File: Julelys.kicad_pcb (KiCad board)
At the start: 4 copper layers, 65 x 56 mm, 118 parts, among them J1 Raspberry_Pi_40pin, J10 B3B-XH-A, J11 B3B-XH-A, J12 Conn_01x03_Pin, J13 FAN, J3 Conn_02x06_Odd_Even, J4 B3B-XH-A, J5 B3B-XH-A, J6 B3B-XH-A, J7 B3B-XH-A, J8 B3B-XH-A, J9 B3B-XH-A, P1 USB_C_Receptacle_USB2.0, Q1 AO3400A, SW1 SW_Push, SW2 SW_Push, U1 ESP32-C3-WROOM-02, U10 74LVC1G08, U2 74HC4051, U3 AMS1117-3.3, U4 BC847BDW1T1G, U5 CP2102N-A02-GQFN28, U6 74AHCT1G125, U7 74AHCT1G125, U8 74AHCT1G125, U9 74AHCT1G125

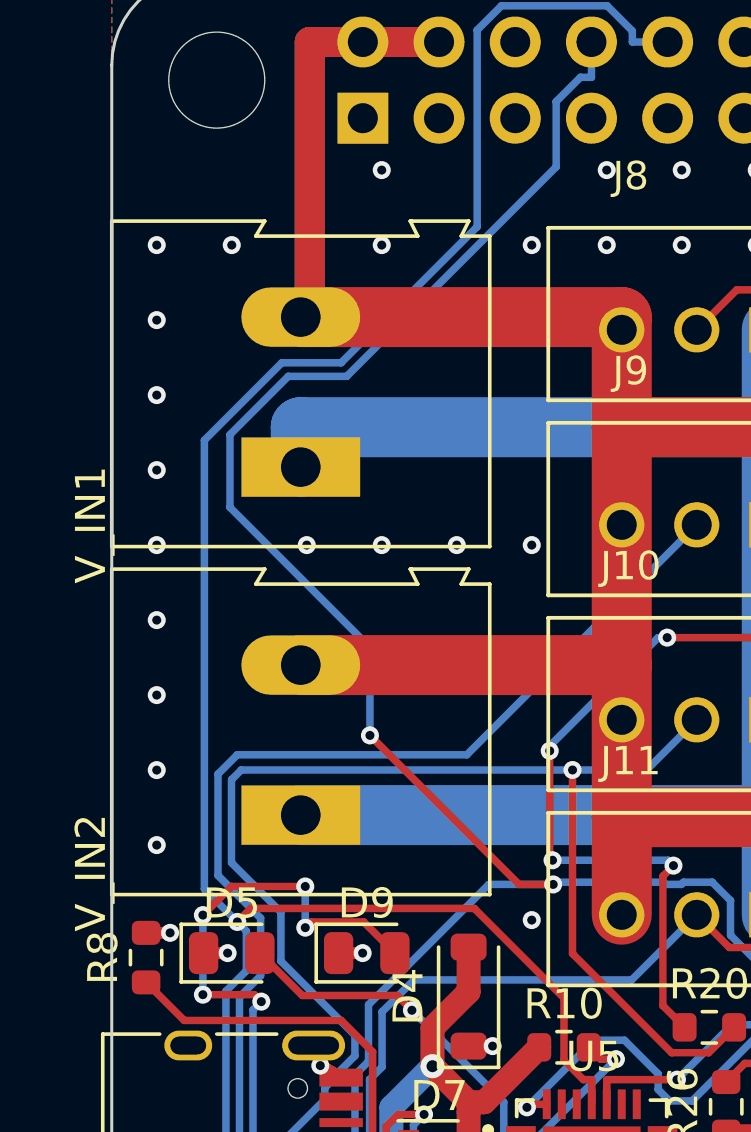
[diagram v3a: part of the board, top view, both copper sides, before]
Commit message: Add 3D models for all parts, turn screw terminals to face the board edge
- Point library parts at KiCad 10 STEP models; copy the HRO USB-C and
  ESP32-C3 models into 3D/ so the project is self-contained
- Add models for U2 (SOIC-16) and U5 (CP2102N); use the KiCad TL3305A
  model instead of a file in Downloads
- Rotate V_IN1/V_IN2 so the 45-degree wire entry faces the left edge;
  mirror the symbols (pin 1 = +5V, pin 2 = GND) so the power tracks stay
- Reroute TXD and PI_TX segments that came too close to the new pads
- Document Pi 5 Active Cooler mounting (GPIO extension, taller standoffs)

Co-Authored-By: Claude Opus 5.5 <noreply@anthropic.com>
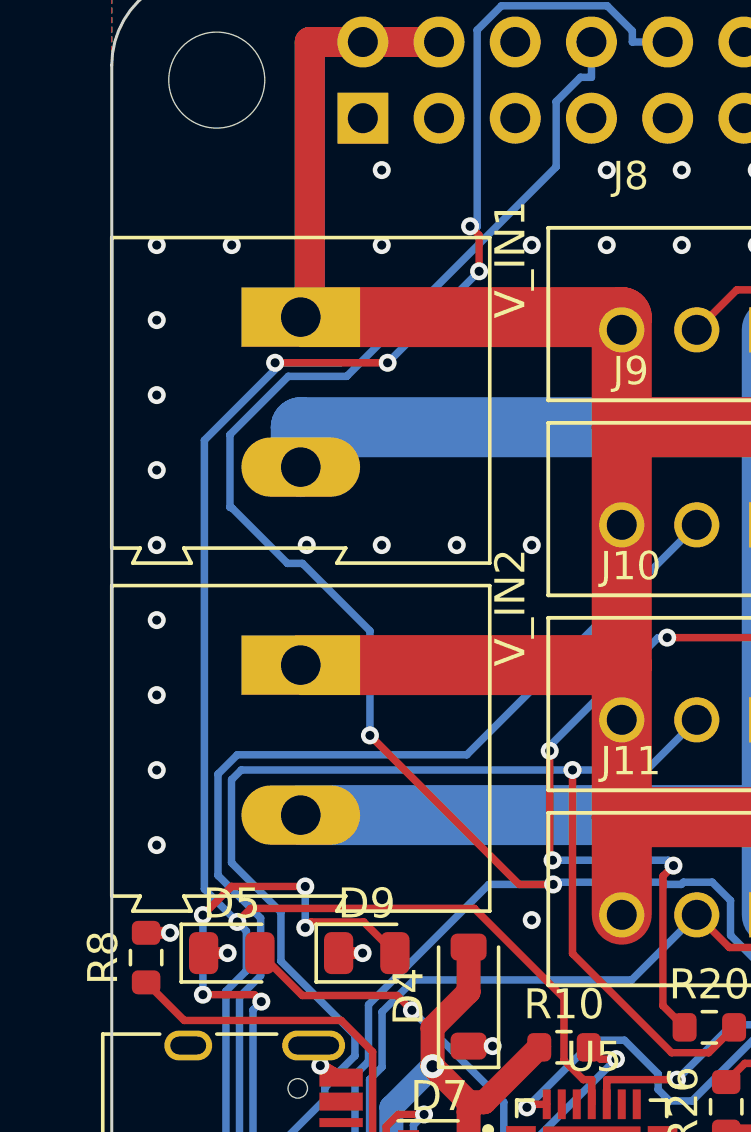
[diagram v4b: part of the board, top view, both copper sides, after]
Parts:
- moved V_IN1 5.00 mm to (26.3, 23.4), turned to -90 degrees
- moved V_IN2 5.00 mm to (26.3, 35.0), turned to -90 degrees
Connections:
- V_IN1 pad 1: GND -> +5V
- V_IN1 pad 2: +5V -> GND
- V_IN2 pad 1: GND -> +5V
- V_IN2 pad 2: +5V -> GND
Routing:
- net TXD: track 100.0 -> 105.8 mm, vias 2 -> 6

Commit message: Match the official HAT mounting hole spec
- Mounting holes 2.75 mm NPTH (was 3.2 mm M3), footprint
  MountingHole_2.7mm_M2.5 in board and schematic
- 6.4 mm copper/track/via keepout around each hole on all layers
  (spec: land min 6.2 mm, not connected to GND)
- Drop the 1 mm Pi 5V track around the left end of J1, which crossed the
  hole land; pins 2/4 are fed by the In2 +5V plane
- Reroute FAN_PWM and CH3 around the top-right hole land
- Document the HAT mechanical spec (65 x 56.0 mm for a THT header)

Co-Authored-By: Claude Opus 5.5 <noreply@anthropic.com>
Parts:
- H1, H2, H3, H4: footprint MountingHole:MountingHole_3.2mm_M3 -> MountingHole:MountingHole_2.7mm_M2.5
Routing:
- net +5V: track 122.0 -> 95.0 mm
- net /CH3: track 71.0 -> 79.8 mm, vias 4 -> 6
- net FAN_PWM: track 73.6 -> 74.0 mm, vias 0 -> 2

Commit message: Move back-side branding under the antenna, add pinout table
- Group the Omega logo, Julelys, Boltehus and version/date in the
  copper-free area under the ESP32 antenna; the logo was hidden under
  the GPIO header and across vias
- Add a mirrored pinout table on the back: V_IN, JST outputs, fan,
  J12, buttons and the J3 GPIO header

Co-Authored-By: Claude Opus 5.5 <noreply@anthropic.com>
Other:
- board text added: "1 +5V 2 GND"
- board text added: "1 FAN- 2 +5V 3 TACH"
- board text added: "1 GND 2 +5V 3 3V3"
- board text added: "1 GND 2 IO8 3 IO9 4 IO6"
- board text added: "5 IO7 6 IO5 7 IO4 8 IO0"
- board text added: "9 IO2 10 IO1 11 IO10 12 IO3"
- board text added: "BOOT (IO9) / RESET (EN)"
- board text added: "CH1-8: 1 GND 2 DATA 3 +5V"
- board text added: "J12"
- board text added: "J13 FAN"
- board text added: "J3"
- board text added: "J4-J11"
- board text added: "PINOUT"
- board text added: "SW1/SW2"
- board text added: "V_IN1/2"

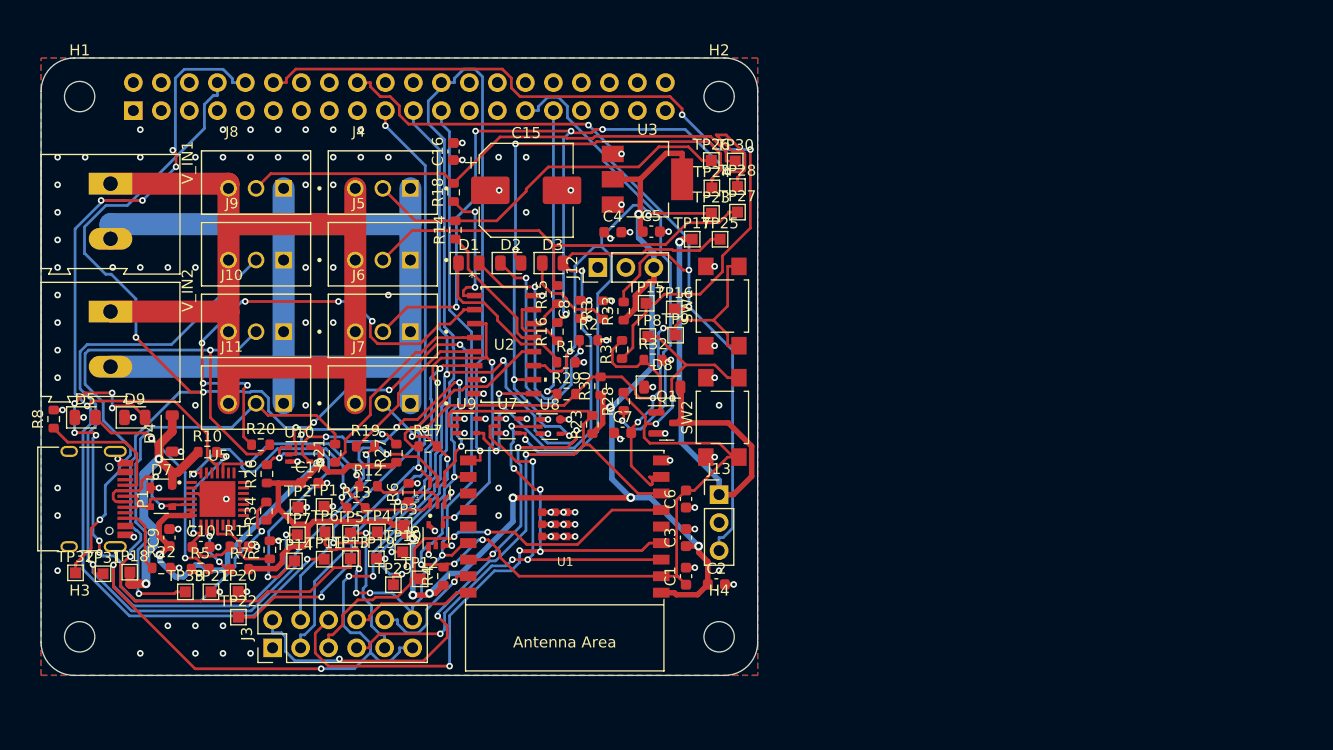
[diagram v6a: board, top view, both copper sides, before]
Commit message: Apply schematic review fixes, add JLCPCB rules, prepare for manual layout
Schematic (from a Codex review):
- R35 10k pull-up on GPIO2 (strapping pin; Pi MISO has a default pull-down)
- R36 10k pull-down on IO7 so the LEDs stay dark while the ESP32 boots
- C5 22uF for AMS1117 output stability, C7 1nF on GPIO9
- C18-C21 100nF decoupling for the level shifters U6-U9

Board:
- New parts parked outside the outline for manual placement
- Silkscreen scaled to JLCPCB's 1.0 mm minimum; back pinout table rebuilt
- C5/C7 values synced

Rules:
- JLCPCB 4-layer limits in Julelys.kicad_pro and new Julelys.kicad_dru

Co-Authored-By: Claude Opus 5.5 <noreply@anthropic.com>
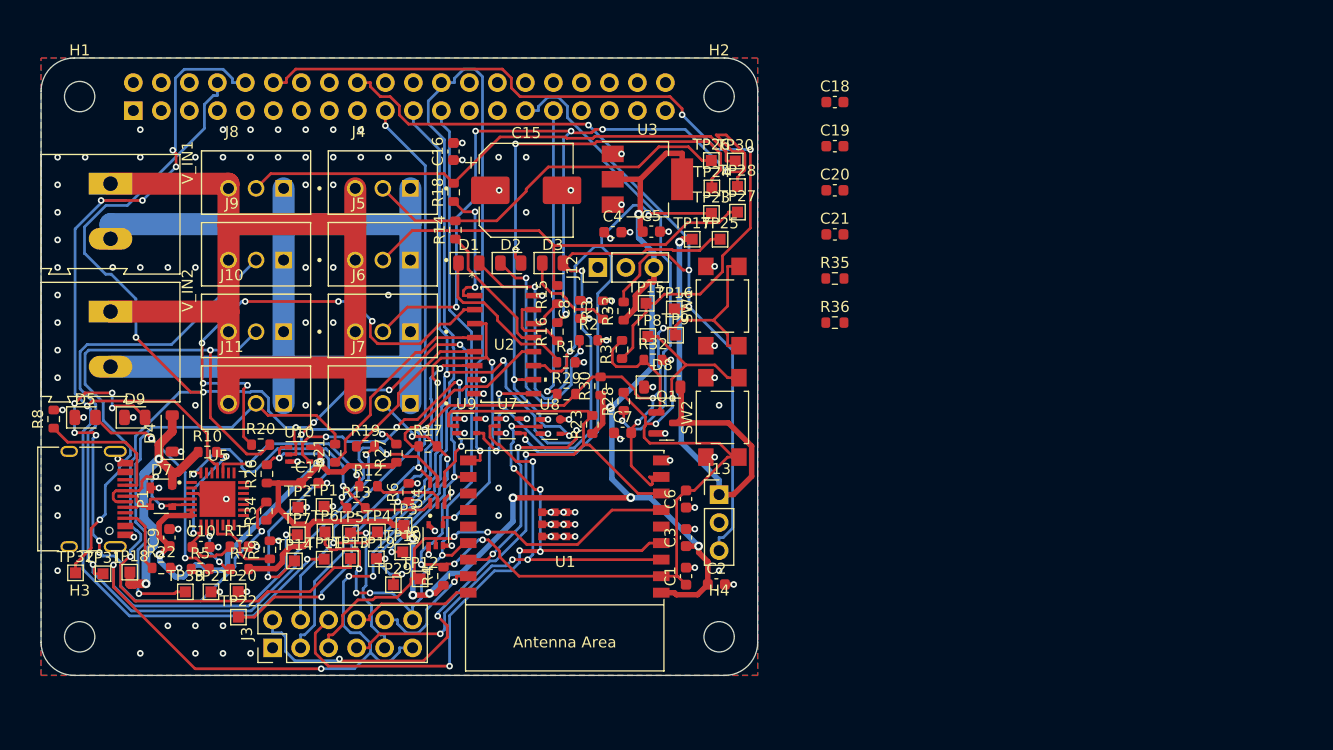
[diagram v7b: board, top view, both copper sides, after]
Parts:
- added C18: 100nF, C_0603_1608Metric, F.Cu at (92.0, 16.0)
- added C19: 100nF, C_0603_1608Metric, F.Cu at (92.0, 20.0)
- added C20: 100nF, C_0603_1608Metric, F.Cu at (92.0, 24.0)
- added C21: 100nF, C_0603_1608Metric, F.Cu at (92.0, 28.0)
- added R35: 10K, R_0603_1608Metric, F.Cu at (92.0, 32.0)
- added R36: 10K, R_0603_1608Metric, F.Cu at (92.0, 36.0)
- C5: value 10uf -> 22uF
- C7: value 0.1uf -> 1nF
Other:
- board text added: "1 GND 2 DATA 3 +5V"
- board text added: "1 GND 2 IO8 3 IO9"
- board text added: "10 IO1 11 IO10 12 IO3"
- board text added: "4 IO6 5 IO7 6 IO5"
- board text added: "7 IO4 8 IO0 9 IO2"
- board text added: "J4-11"
- board text added: "SW1/2"
- board text removed: "1 GND 2 IO8 3 IO9 4 IO6"
- board text removed: "5 IO7 6 IO5 7 IO4 8 IO0"
- board text removed: "9 IO2 10 IO1 11 IO10 12 IO3"
- board text removed: "CH1-8: 1 GND 2 DATA 3 +5V"
- board text removed: "J4-J11"
- board text removed: "SW1/SW2"
